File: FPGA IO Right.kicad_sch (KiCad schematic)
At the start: 29 parts, among them J4 Expansion, J801 Frontpanel, SW3 BTN1, SW4 BTN2, SW5 BTN3, U1 LFE5UM5G-85F-8BG381x

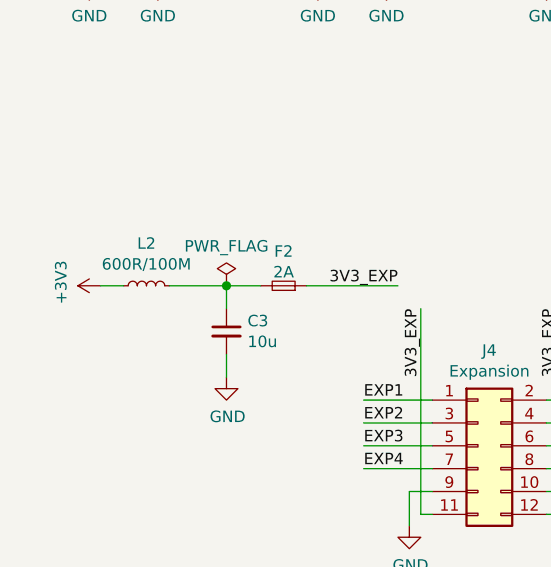
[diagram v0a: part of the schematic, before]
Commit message: Update to KiCad 6
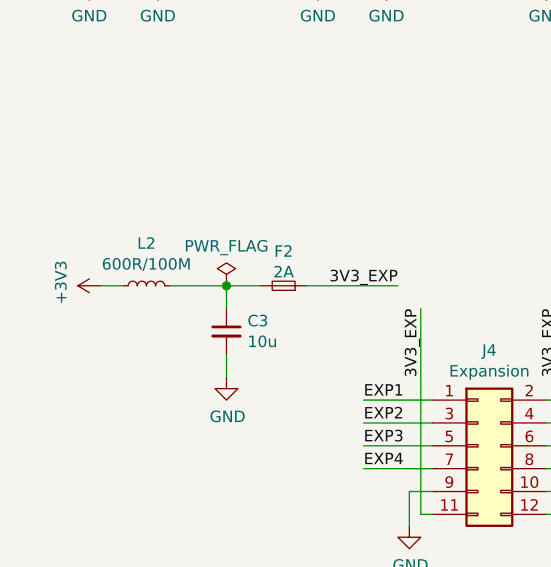
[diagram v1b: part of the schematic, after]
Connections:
- net ~LED_DISPLAY_OE renamed ~{LED_DISPLAY_OE}
- net ~LED_OE renamed ~{LED_OE}
- net ~LED_SW_OE renamed ~{LED_SW_OE}
- net ~POTI_CS renamed ~{POTI_CS}
- net ~SW_SER_CE renamed ~{SW_SER_CE}
- net ~SW_SER_PL renamed ~{SW_SER_PL}
